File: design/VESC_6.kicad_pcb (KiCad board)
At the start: 4 copper layers, 60 x 60 mm, 305 parts, among them P1 USB_OTG, P10 PH_C, P11 SUPPLY, P12 GND, P2 BATT_-, P2 CAN, P4 HALL_ENC, P5 COM, P6 SERVO, P7 SWD, P8 PH_A, P9 PH_B, Q1 IRF7749, Q2 IRF7749, Q3 IRF7749, Q4 IRF7749, Q5 IRF7749, Q6 IRF7749, U1 STM32F40X_LQFP64, U10 MPU9150, U11 SENSOR_VOLTAGE, U2 LM3671, U3 DRV8301, U4 TJA1051TK3, U5 AD8418, U6 AD8418, U7 AD8418, U8 NRF24L01P, U9 CONN_U_FL, X1 8m, X2 16M

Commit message: TESC 1.2
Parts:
- moved C7 0.06 mm to (133.1, 99.2)

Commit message: TESC 1.3
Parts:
- Sensor Voltage: renamed from U11
- moved C13 3.70 mm to (127.6, 79.0)
- moved C1 1.33 mm to (121.7, 96.7)
- moved R6 1.33 mm to (121.7, 98.1)
- moved C3 1.21 mm to (126.6, 97.4)
- moved C42 1.09 mm to (126.2, 64.3)
- moved U7 1.09 mm to (128.8, 64.3)
- moved C38 0.81 mm to (131.6, 63.2)
- moved U6 0.81 mm to (134.2, 63.2)
- moved C35 0.65 mm to (136.5, 67.8)
- moved U5 0.65 mm to (139.1, 65.8)
- moved D4 0.64 mm to (124.1, 62.2)
- moved C14 0.54 mm to (123.9, 72.6)
- moved C15 0.54 mm to (123.9, 74.0)
- moved C16 0.54 mm to (125.5, 69.7)
- moved C17 0.54 mm to (125.3, 77.6)
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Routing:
- net /DRV8301/SCLK: track 33.3 -> 45.2 mm
- net /nrf/MOSI: track 31.3 -> 42.5 mm
- net GND: track 318.7 -> 314.2 mm
- net VCC: track 227.1 -> 223.4 mm
- net /MCU/ADC_TEMP: track 27.5 -> 30.4 mm
- net Net-(R32-Pad3): track 48.8 -> 46.7 mm
- net /Power/C_C: track 43.7 -> 41.7 mm
- net Net-(C28-Pad2): track 20.4 -> 18.9 mm
- net /Power/C_A: track 51.1 -> 52.4 mm
- net SUPPLY: track 45.9 -> 44.8 mm
- net Net-(Q2-PadG): track 11.7 -> 10.6 mm
- net /MCU/RX_SDA_NSS: track 22.4 -> 23.5 mm
- net Net-(R32-Pad4): track 49.6 -> 48.6 mm
- net /CAN/CANL: track 8.13 -> 9.07 mm
- net /DRV8301/SDO: track 30.7 -> 31.7 mm
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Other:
- outline, holes or cut-outs redrawn

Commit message: TESC 1.4
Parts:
- moved C38 0.38 mm to (132.0, 63.2)
- moved U6 0.38 mm to (134.5, 63.2)
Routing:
- net VCC: track 223.4 -> 210.2 mm, vias 12 -> 13
- net /MCU/TEMP_MOTOR: track 54.6 -> 51.6 mm, vias 2 -> 1
- net /MCU/HALL_1: track 71.2 -> 73.1 mm
- net Net-(R24-Pad4): track 11.7 -> 12.5 mm
- net +5V: track 138.3 -> 139.0 mm
- net Net-(R29-Pad4): track 29.6 -> 29.0 mm

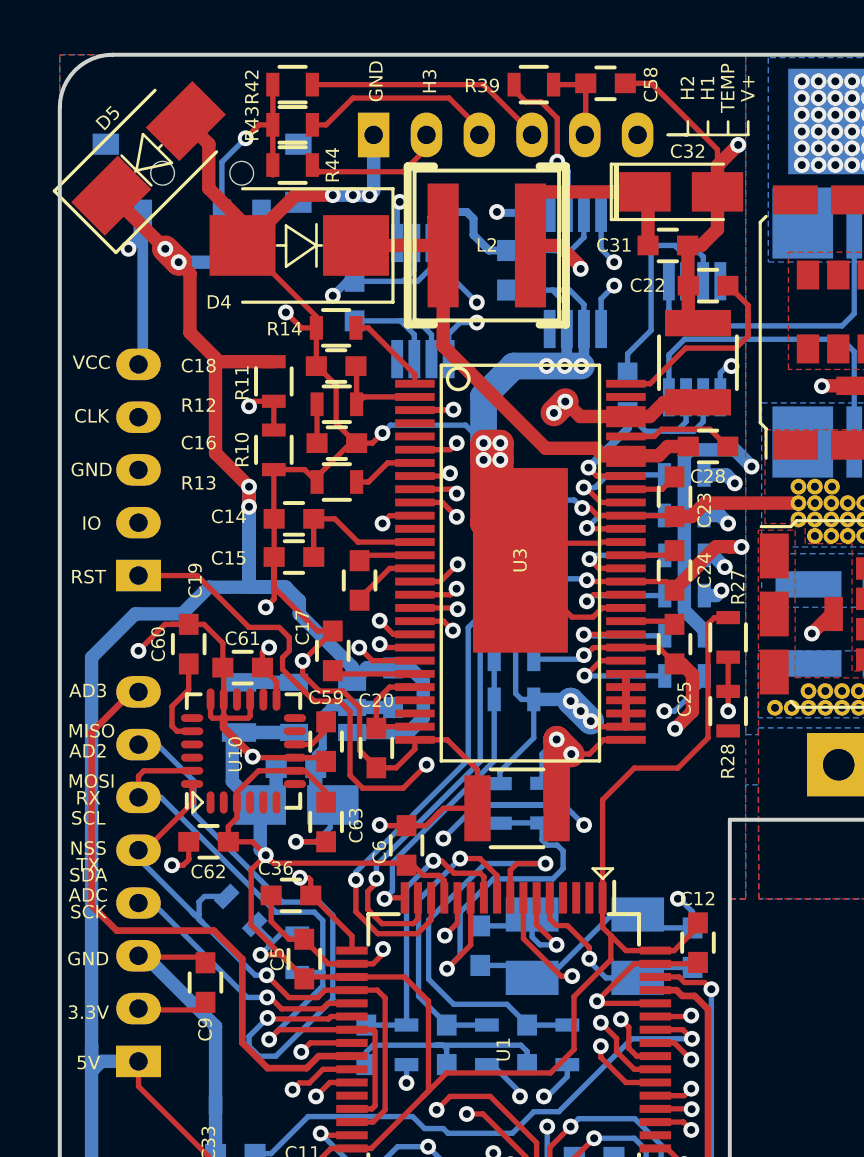
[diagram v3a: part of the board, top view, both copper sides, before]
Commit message: Make Loops Small
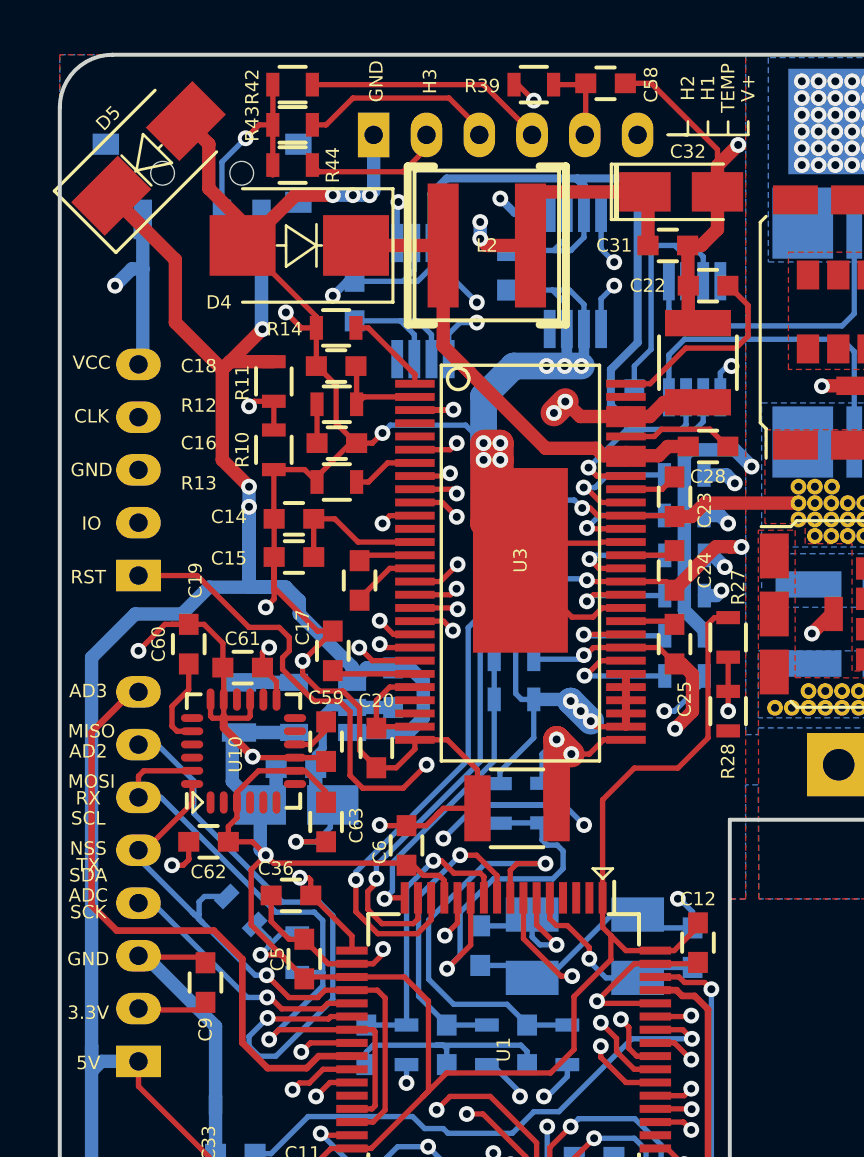
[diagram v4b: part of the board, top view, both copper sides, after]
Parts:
- moved C35 0.68 mm to (136.8, 68.5)
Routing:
- net VCC: track 210.2 -> 220.5 mm
- net /Power/C_B: track 47.7 -> 50.0 mm
- net +5V: track 139.0 -> 137.4 mm
- net /MCU/TEMP_MOTOR: track 51.6 -> 52.7 mm
- net /MCU/HALL_1: track 73.1 -> 74.0 mm
- net GND: track 313.9 -> 314.4 mm

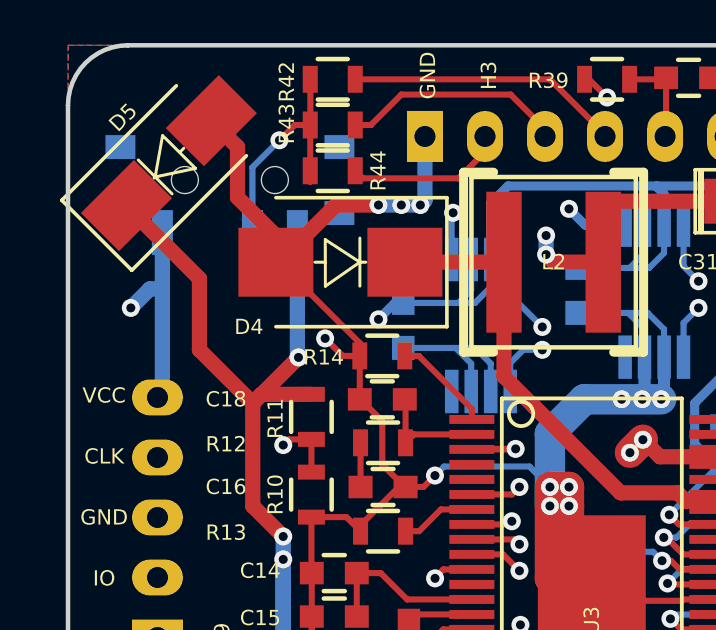
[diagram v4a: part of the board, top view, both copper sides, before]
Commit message: Make Loops Small
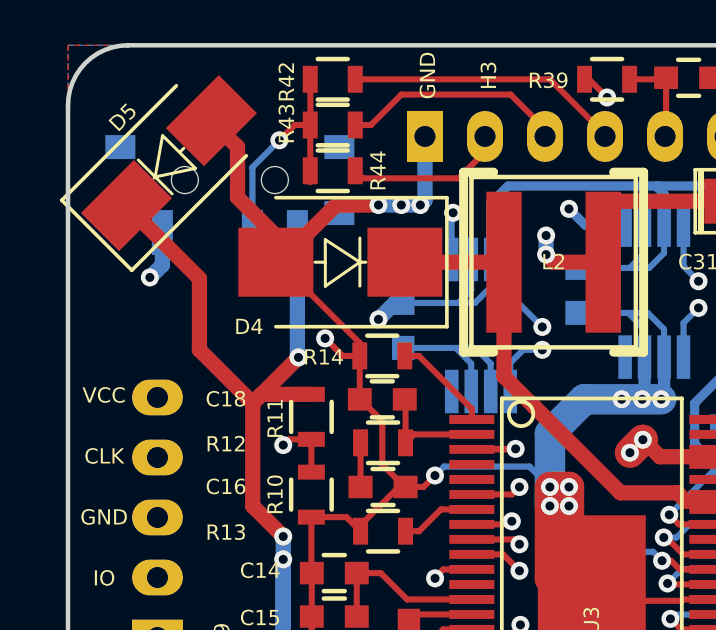
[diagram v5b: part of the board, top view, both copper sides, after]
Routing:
- net VCC: track 220.5 -> 215.7 mm
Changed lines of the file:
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@@
     (thickness 1.6)
     (drawings 113)
-    (tracks 2038)
+    (tracks 2037)
     (zones 0)
     (modules 305)
@@
     (44 Edge.Cuts user)
     (45 Margin user)
-    (46 B.CrtYd user hide)
+    (46 B.CrtYd user)
     (47 F.CrtYd user)
-    (48 B.Fab user hide)
-    (49 F.Fab user hide)
+    (48 B.Fab user)
+    (49 F.Fab user)
   )
   (setup
-    (last_trace_width 0.3048)
+    (last_trace_width 0.508)
     (user_trace_width 0.2032)
     (user_trace_width 0.254)
@@
   (segment (start 135.001 100.0125) (end 135.076001 99.937499) (width 0.2032) (layer F.Cu) (net 5) (status 30))
   (segment (start 135.076001 99.937499) (end 135.076001 98.459999) (width 0.2032) (layer F.Cu) (net 5) (status 30))
+  (segment (start 126.1745 63.5875) (end 125.8965 63.5875) (width 0.508) (layer B.Cu) (net 6) (status 30))
+  (segment (start 125.8965 63.5875) (end 125.349 64.135) (width 0.508) (layer B.Cu) (net 6) (status 10))
+  (segment (start 118.146 61.242) (end 118.146 62.321) (width 0.508) (layer B.Cu) (net 6) (status 10))
+  (segment (start 118.146 62.321) (end 117.729 62.738) (width 0.508) (layer B.Cu) (net 6))
+  (via (at 117.729 62.738) (size 0.6) (drill 0.3) (layers F.Cu B.Cu) (net 6))
+  (segment (start 118.11 66.6115) (end 117.983 66.7385) (width 0.508) (layer B.Cu) (net 6) (status 30))
   (segment (start 134.62 59.69) (end 129.667 59.69) (width 0.3048) (layer B.Cu) (net 6))
   (segment (start 129.0903 60.2667) (end 129.0903 62.1382) (width 0.3048) (layer B.Cu) (net 6) (status 20))
@@
   (segment (start 132.365658 56.134) (end 132.970992 56.739334) (width 0.2032) (layer F.Cu) (net 6) (status 10))
   (via (at 132.970992 56.739334) (size 0.6) (drill 0.3) (layers F.Cu B.Cu) (net 6))
-  (segment (start 118.146 63.119) (end 118.146 66.5755) (width 0.508) (layer B.Cu) (net 6) (status 20))
-  (segment (start 118.146 61.242) (end 118.146 63.119) (width 0.508) (layer B.Cu) (net 6) (status 10))
-  (segment (start 118.146 63.119) (end 117.729 63.119) (width 0.508) (layer B.Cu) (net 6))
-  (segment (start 117.729 63.119) (end 117.094 63.754) (width 0.508) (layer B.Cu) (net 6))
-  (via (at 117.094 63.754) (size 0.6) (drill 0.3) (layers F.Cu B.Cu) (net 6))
   (segment (start 118.146 66.5755) (end 117.983 66.7385) (width 0.508) (layer B.Cu) (net 6) (status 30))
   (segment (start 117.983 66.7385) (end 117.0305 66.7385) (width 0.508) (layer GND.Cu) (net 6) (status 10))
@@
   (segment (start 116.205 90.424) (end 116.93906 91.15806) (width 0.508) (layer GND.Cu) (net 6))
   (segment (start 116.93906 91.15806) (end 117.983 91.15806) (width 0.508) (layer GND.Cu) (net 6) (status 20))
-  (segment (start 126.1745 63.5875) (end 125.8965 63.5875) (width 0.3048) (layer B.Cu) (net 6) (status 30))
-  (segment (start 125.8965 63.5875) (end 125.349 64.135) (width 0.3048) (layer B.Cu) (net 6) (status 10))
   (segment (start 122.599 83.439) (end 122.599 85.134) (width 0.508) (layer B.Cu) (net 6) (status 10))
   (segment (start 122.599 85.134) (end 122.809 85.344) (width 0.508) (layer B.Cu) (net 6))

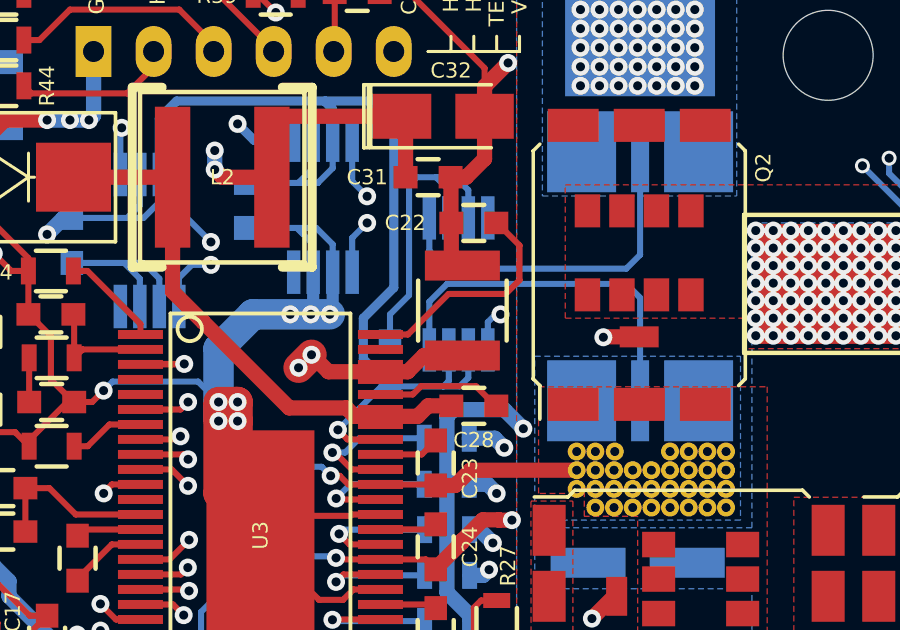
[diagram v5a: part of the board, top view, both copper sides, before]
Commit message: Make Loops Small
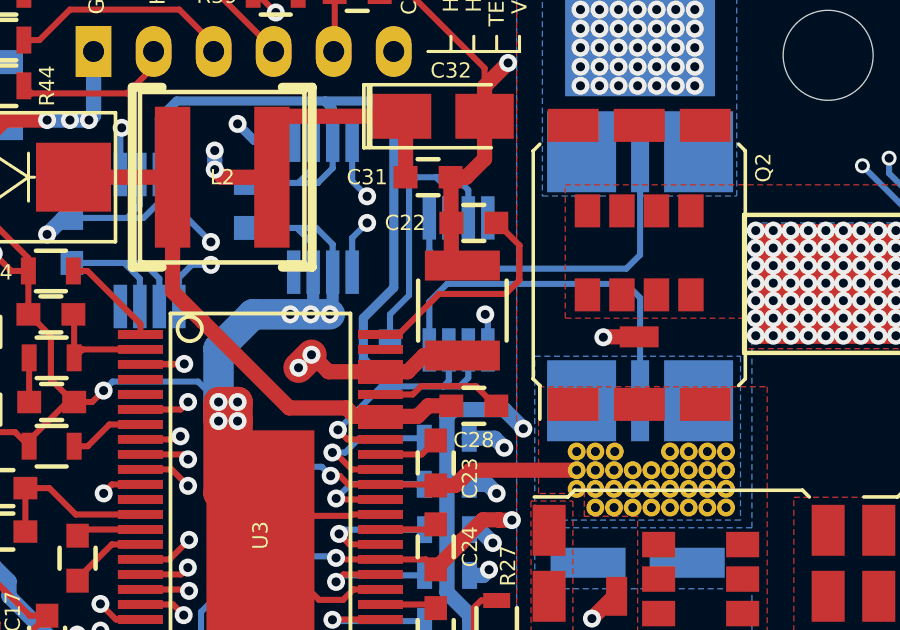
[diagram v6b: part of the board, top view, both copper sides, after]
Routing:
- net /Power/C_A: track 52.5 -> 51.7 mm
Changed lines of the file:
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@@
     (44 Edge.Cuts user)
     (45 Margin user)
-    (46 B.CrtYd user)
-    (47 F.CrtYd user)
-    (48 B.Fab user)
-    (49 F.Fab user)
+    (46 B.CrtYd user hide)
+    (47 F.CrtYd user hide)
+    (48 B.Fab user hide)
+    (49 F.Fab user hide)
   )
   (setup
-    (last_trace_width 0.508)
+    (last_trace_width 0.2032)
     (user_trace_width 0.2032)
     (user_trace_width 0.254)
@@
   (segment (start 127.50673 78.97114) (end 127 79.47787) (width 0.2032) (layer F.Cu) (net 16))
   (segment (start 127 79.47787) (end 127 80.542) (width 0.2032) (layer F.Cu) (net 16) (status 20))
-  (segment (start 136.4615 67.47256) (end 137.37844 67.47256) (width 0.2032) (layer F.Cu) (net 17) (status 10))
-  (segment (start 137.37844 67.47256) (end 138.730001 66.120999) (width 0.2032) (layer F.Cu) (net 17))
+  (segment (start 140.348 63.754) (end 140.323 63.754) (width 0.2032) (layer F.Cu) (net 17))
+  (segment (start 141.097 64.503) (end 140.348 63.754) (width 0.2032) (layer F.Cu) (net 17))
   (segment (start 141.097 65.659) (end 141.097 64.503) (width 0.2032) (layer F.Cu) (net 17))
-  (segment (start 138.730001 66.120999) (end 140.635001 66.120999) (width 0.2032) (layer F.Cu) (net 17))
-  (segment (start 140.635001 66.120999) (end 141.097 65.659) (width 0.2032) (layer F.Cu) (net 17))
-  (segment (start 141.097 64.503) (end 140.348 63.754) (width 0.2032) (layer F.Cu) (net 17) (status 20))
-  (segment (start 140.348 63.754) (end 140.323 63.754) (width 0.2032) (layer F.Cu) (net 17) (status 30))
+  (segment (start 136.4615 67.47256) (end 137.06221 67.47256) (width 0.2032) (layer F.Cu) (net 17))
+  (segment (start 138.413781 66.120989) (end 140.635011 66.120989) (width 0.2032) (layer F.Cu) (net 17))
+  (segment (start 140.635011 66.120989) (end 141.097 65.659) (width 0.2032) (layer F.Cu) (net 17))
+  (segment (start 137.06221 67.47256) (end 138.413781 66.120989) (width 0.2032) (layer F.Cu) (net 17))
   (segment (start 136.4615 71.47052) (end 137.83748 71.47052) (width 0.2032) (layer F.Cu) (net 18) (status 10))
   (segment (start 137.83748 71.47052) (end 138.303 71.005) (width 0.2032) (layer F.Cu) (net 18) (status 20))
@@
   (segment (start 134.940998 78.537112) (end 134.88964 78.537112) (width 0.2032) (layer F.Cu) (net 81))
   (via (at 134.88964 78.537112) (size 0.6) (drill 0.3) (layers F.Cu B.Cu) (net 81))
-  (segment (start 133.349996 94.488) (end 132.460996 93.599) (width 0.2032) (layer GND.Cu) (net 82))
-  (segment (start 129.413 66.04) (end 139.7 66.04) (width 0.2032) (layer GND.Cu) (net 82))
-  (segment (start 132.460996 93.599) (end 130.048 93.599) (width 0.2032) (layer GND.Cu) (net 82))
+  (segment (start 121.539 73.914) (end 129.413 66.04) (width 0.2032) (layer GND.Cu) (net 82))
+  (segment (start 129.413 66.04) (end 139.191998 66.04) (width 0.2032) (layer GND.Cu) (net 82))
   (segment (start 130.048 93.599) (end 121.539 85.09) (width 0.2032) (layer GND.Cu) (net 82))
   (segment (start 121.539 85.09) (end 121.539 73.914) (width 0.2032) (layer GND.Cu) (net 82))
-  (segment (start 121.539 73.914) (end 129.413 66.04) (width 0.2032) (layer GND.Cu) (net 82))
-  (segment (start 139.7 66.04) (end 140.462 66.802) (width 0.2032) (layer GND.Cu) (net 82))
-  (segment (start 140.04 67.986) (end 140.04 67.0578) (width 0.2032) (layer B.Cu) (net 82) (status 10))
-  (segment (start 140.2958 66.802) (end 140.462 66.802) (width 0.2032) (layer B.Cu) (net 82))
-  (segment (start 140.04 67.0578) (end 140.2958 66.802) (width 0.2032) (layer B.Cu) (net 82))
-  (via (at 140.462 66.802) (size 0.6) (drill 0.3) (layers F.Cu B.Cu) (net 82))
+  (segment (start 132.460996 93.599) (end 130.048 93.599) (width 0.2032) (layer GND.Cu) (net 82))
+  (segment (start 140.04 67.986) (end 140.04 66.888002) (width 0.2032) (layer B.Cu) (net 82))
+  (segment (start 139.653999 66.502001) (end 139.953998 66.802) (width 0.2032) (layer GND.Cu) (net 82))
+  (segment (start 139.191998 66.04) (end 139.653999 66.502001) (width 0.2032) (layer GND.Cu) (net 82))
+  (segment (start 133.349996 94.488) (end 132.460996 93.599) (width 0.2032) (layer GND.Cu) (net 82))
+  (segment (start 140.04 66.888002) (end 139.953998 66.802) (width 0.2032) (layer B.Cu) (net 82))
+  (via (at 139.953998 66.802) (size 0.6) (drill 0.3) (layers F.Cu B.Cu) (net 82))
   (segment (start 133.4864 94.488) (end 133.349996 94.488) (width 0.2032) (layer B.Cu) (net 82))
   (segment (start 134.239 93.7354) (end 133.4864 94.488) (width 0.2032) (layer B.Cu) (net 82))
